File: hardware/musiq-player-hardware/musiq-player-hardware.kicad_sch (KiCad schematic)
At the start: 16 parts, among them SW1 SW_MEC_5E, SW2 SW_MEC_5E, SW3 SW_MEC_5E, SW4 SW_MEC_5E, SW5 SW_MEC_5E, U2 ESP32-PICO-D4

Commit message: adds sd card module and esp-pico-d4
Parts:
- removed U2: ESP32-PICO-D4, Package_DFN_QFN:QFN-48-1EP_7x7mm_P0.5mm_EP5.3x5.3mm, symbol RF_Module:ESP32-PICO-D4
- added C6, C7: 100nF, symbol Device:C_Small
- added J1: Micro_SD_Card, symbol Connector:Micro_SD_Card
- added R6, R7, R8, R9: 3.3k, symbol Device:R_US
- added U1: 74LVC125, symbol 74xx:74LVC125
- added U3: ~, symbol custom-modules:OLED-0.96{dblquote}
- added U4: ESP32-PICO-D4, Package_DFN_QFN:QFN-48-1EP_7x7mm_P0.5mm_EP5.3x5.3mm, symbol RF_Module:ESP32-PICO-D4
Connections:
- net +3V3: now also C6.1, C7.1, J1.4 (VDD), U1.14 (VCC), U4.1 (VDDA), U4.3 (VDDA3P3), U4.4 (VDDA3P3), U4.43 (VDDA), U4.46 (VDDA)
- net GND: now also C6.2, C7.2, J1.6 (VSS), J1.9 (SHIELD), U1.1, U1.10, U1.13, U1.4, U1.7 (GND), U4.49 (GND)
- new net: J1.2 (DAT3/CD), U1.8
- new net: R8.2, U1.9
- new net: R7.2, U1.5
- new net: R6.2, U1.2
- new net: J1.3 (CMD), U1.3
- new net: J1.7 (DAT0), R9.1
- new net: R9.2, U1.12
- new net: J1.5 (CLK), U1.6
- new net CS: R8.1
- new net MISO: U1.11
- new net MOSI: R6.1, R7.1
- no-connect marks 10 -> 12
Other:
- note removed: "OLED"
- note removed: "SDCARD MODULE"
- moved on the sheet: C1, C2, C3, C4, C5, R1, R2, R3, R4, R5, SW1, SW2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

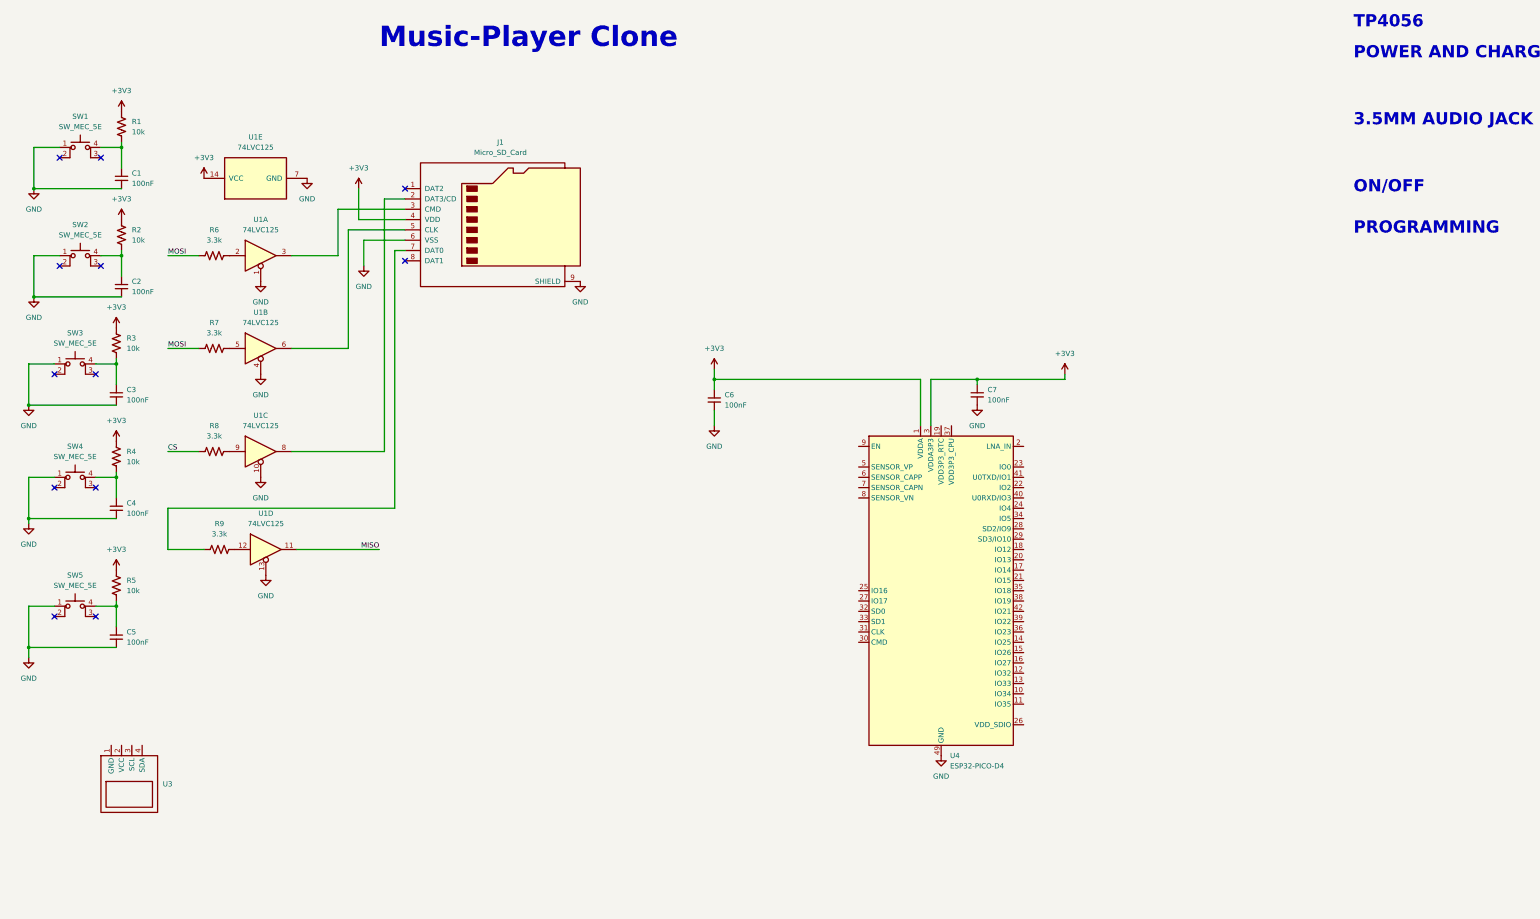
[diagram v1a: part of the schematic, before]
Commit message: adds on/off switch schematic
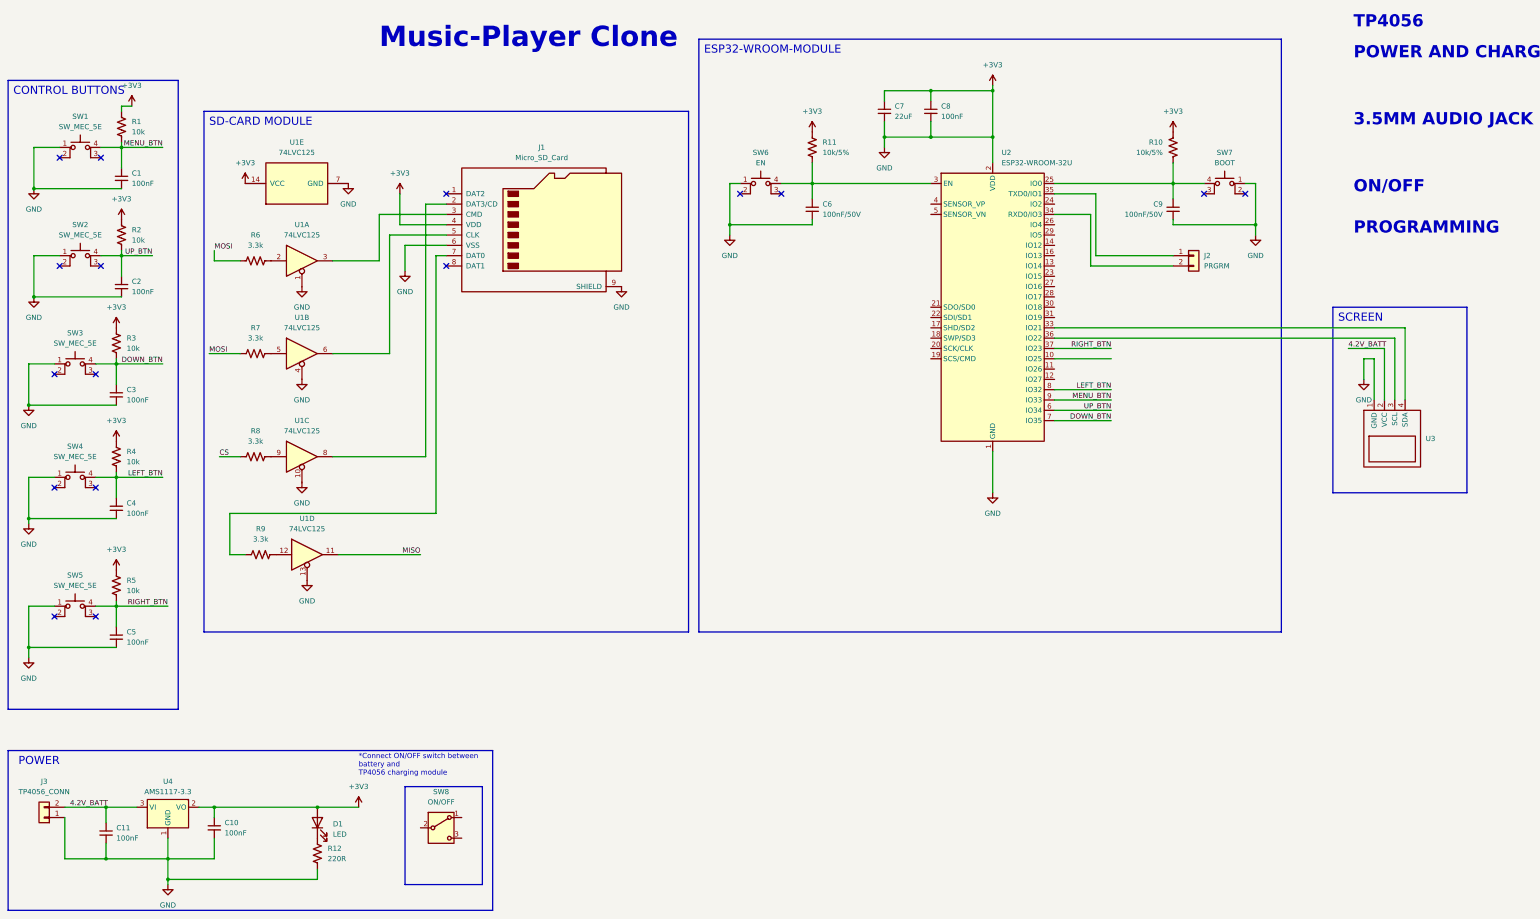
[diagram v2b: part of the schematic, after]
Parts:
- removed U4: ESP32-PICO-D4, Package_DFN_QFN:QFN-48-1EP_7x7mm_P0.5mm_EP5.3x5.3mm, symbol RF_Module:ESP32-PICO-D4
- added C10, C11, C8: 100nF, symbol Device:C_Small
- added C9: 100nF/50V, symbol Device:C_Small
- added D1: LED, symbol Device:LED
- added J2: PRGRM, symbol Connector_Generic:Conn_01x02
- added J3: TP4056_CONN, symbol Connector_Generic:Conn_01x02
- added R10, R11: 10k/5%, symbol Device:R_US
- added R12: 220R, symbol Device:R_US
- added SW6: EN, symbol Switch:SW_MEC_5E
- added SW7: BOOT, symbol Switch:SW_MEC_5E
- added SW8: ON/OFF, symbol Switch:SW_SPDT
- added U2: ESP32-WROOM-32U, RF_Module:ESP32-WROOM-32U, symbol RF_Module:ESP32-WROOM-32U
- added U4: AMS1117-3.3, Package_TO_SOT_SMD:SOT-223-3_TabPin2, symbol Regulator_Linear:AMS1117-3.3
- C6: value 100nF -> 100nF/50V
- C7: value 100nF -> 22uF
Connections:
- net GND is gone; now on net +3V3: C1.2, C2.2, C3.2, C4.2, C5.2, C6.2, C7.2, J1.6 (VSS), J1.9 (SHIELD), SW1.1, SW2.1, SW3.1, SW4.1, SW5.1, U1.1, U1.10, U1.13, U1.4, U1.7 (GND)
- net +3V3: now also U3.1 (GND), C10.1, C10.2, C11.2, C8.1, C8.2, C9.2, D1.2 (A), J3.1 (Pin_1), R10.1, R11.1, R12.2, SW6.1, SW7.1, U2.1 (GND), U2.15 (GND), U2.2 (VDD), U2.38 (GND), U2.39 (GND), U4.1 (GND), U4.2 (VO); no longer C6.1
- net RIGHT_BTN: now reaches C5.1, R5.2, SW5.4 (A)
- net RIGHT_BTN: now also U2.37 (IO23)
- net LEFT_BTN: now reaches C4.1, R4.2, SW4.4 (A)
- net LEFT_BTN: now also U2.8 (IO32)
- net UP_BTN: now reaches C2.1, R2.2, SW2.4 (A)
- net UP_BTN: now also U2.6 (IO34)
- net MENU_BTN: now reaches C1.1, R1.2, SW1.4 (A)
- net MENU_BTN: now also U2.9 (IO33)
- net DOWN_BTN: now reaches C3.1, R3.2, SW3.4 (A)
- net DOWN_BTN: now also U2.7 (IO35)
- net 4.2V_BATT: now reaches U3.2 (VCC)
- net 4.2V_BATT: now also C11.1, J3.2 (Pin_2), U4.3 (VI)
- net at U3.3 (SCL): now also U2.36 (IO22)
- net at U3.4 (SDA): now also U2.33 (IO21)
- new net: C6.1, R11.2, SW6.4 (A), U2.3 (EN)
- new net: D1.1 (K), R12.1
- new net: C9.1, R10.2, SW7.4 (A), U2.25 (IO0)
- new net: J2.1 (Pin_1), U2.35 (TXD0/IO1)
- new net: J2.2 (Pin_2), U2.34 (RXD0/IO3)
- no-connect marks 12 -> 16
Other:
- note added: "*Connect ON/OFF switch between battery and TP4056 charging module"
- note added: "CONTROL BUTTONS"
- note added: "ESP32-WROOM-MODULE"
- note added: "POWER"
- note added: "SCREEN"
- note added: "SD-CARD MODULE"
- moved on the sheet: J1, R6, R7, R8, R9, U1A, U1B, U1C, U1D, U1E, U3

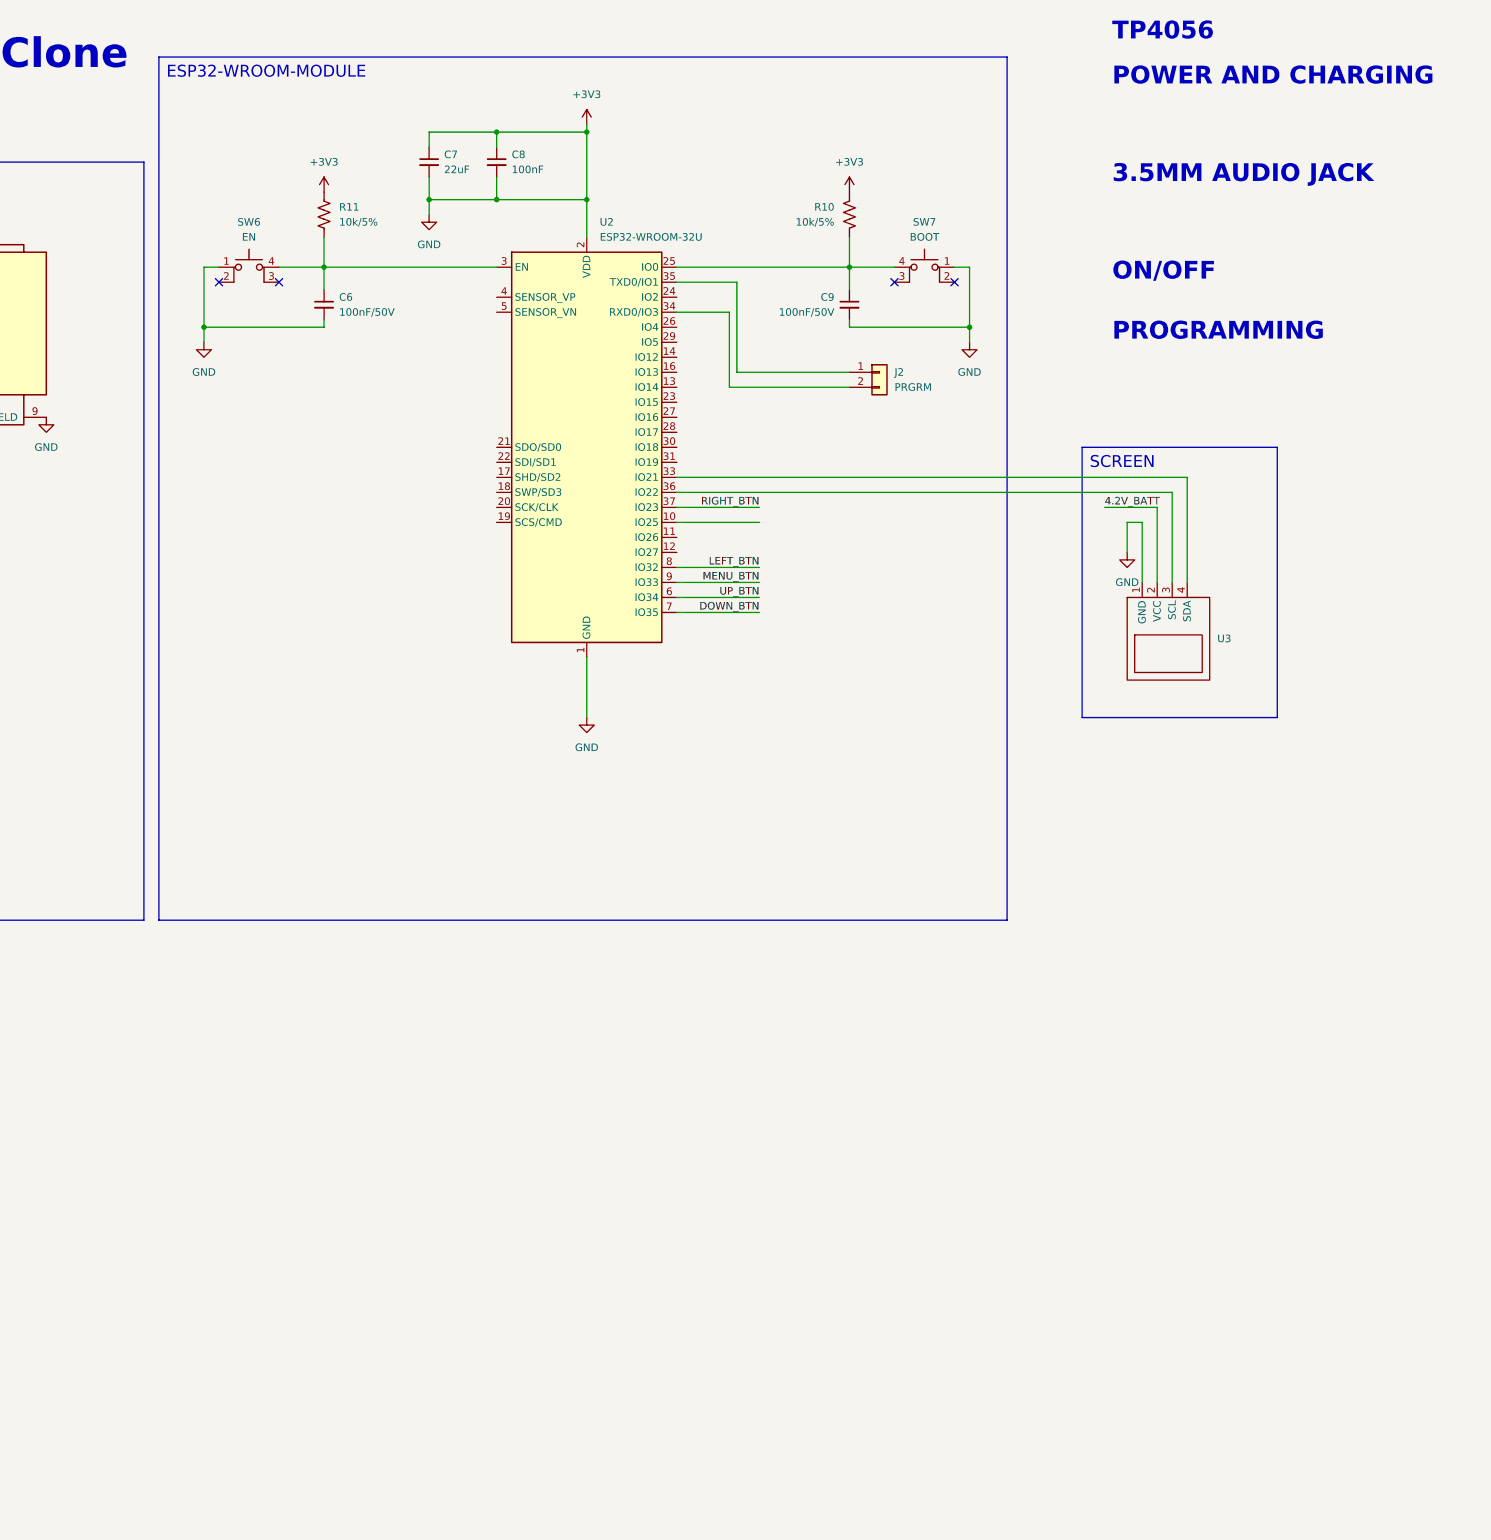
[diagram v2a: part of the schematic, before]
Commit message: adds esp32-c3 schematic
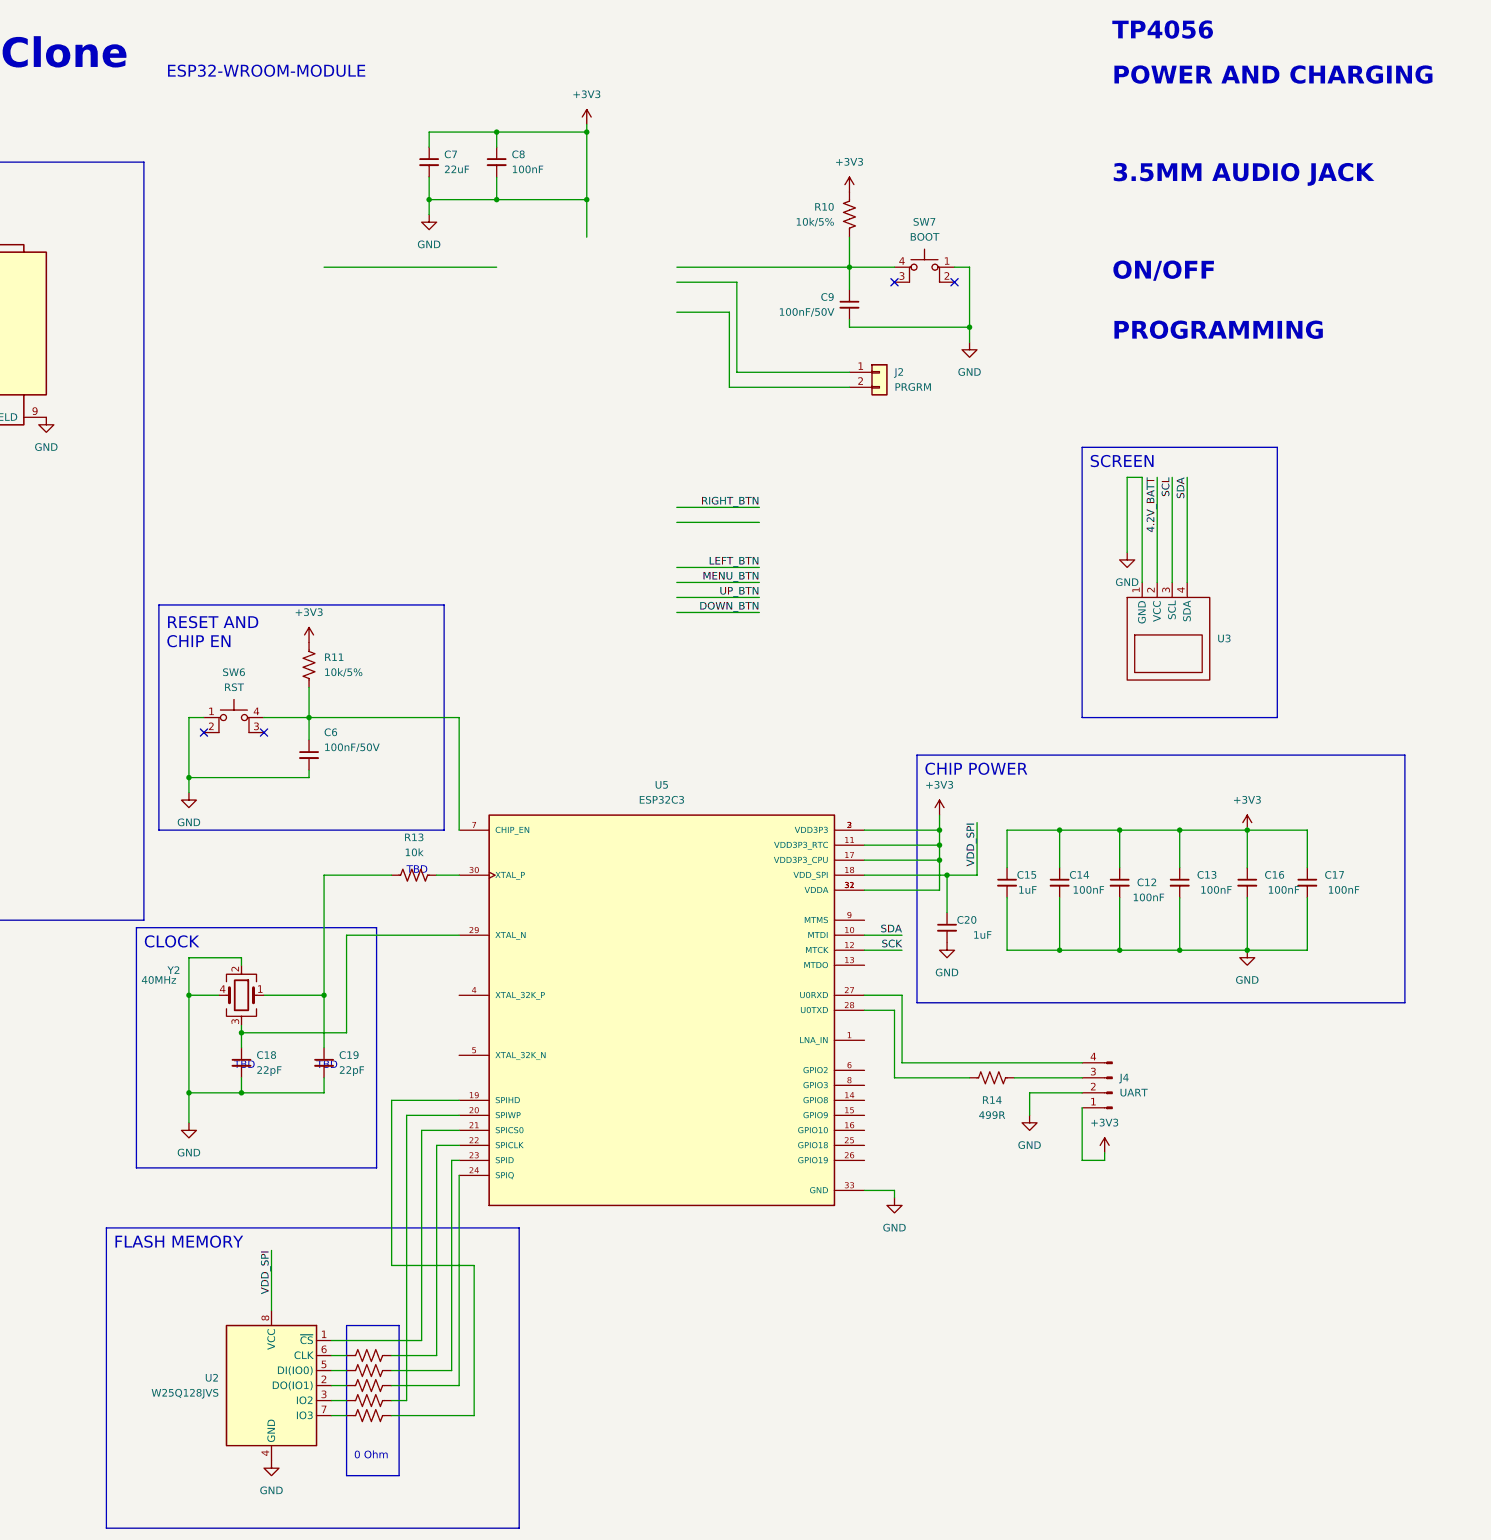
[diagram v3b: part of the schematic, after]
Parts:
- removed U2: ESP32-WROOM-32U, RF_Module:ESP32-WROOM-32U, symbol RF_Module:ESP32-WROOM-32U
- added C12, C13, C14, C16, C17: 100nF, symbol Device:C_Small
- added C15, C20: 1uF, symbol Device:C_Small
- added C18, C19: 22pF, symbol Device:C_Small
- added J4: UART, symbol Connector:Conn_01x04_Pin
- added R13, R16, R17, R18, R19, R20: 10k, symbol Device:R_US
- added R14: 499R, symbol Device:R_US
- added U2: W25Q128JVS, Package_SO:SOIC-8_5.23x5.23mm_P1.27mm, symbol Memory_Flash:W25Q128JVS
- added U5: ESP32C3, ESP32C3:QFN32_5X5MM, symbol ESP32C3:ESP32C3
- added Y2: 40MHz, symbol Device:Crystal_GND23
- SW6: value EN -> RST
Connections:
- net +3V3: now also C12.1, C12.2, C13.1, C13.2, C14.1, C14.2, C15.1, C15.2, C16.1, C16.2, C17.1, C17.2, C18.2, C19.2, C20.2, J4.1 (Pin_1), J4.2 (Pin_2), U2.4 (GND), U5.11 (VDD3P3_RTC), U5.17 (VDD3P3_CPU), U5.2 (VDD3P3), U5.3 (VDD3P3), U5.31 (VDDA), U5.32 (VDDA), U5.33 (GND), Y2.2, Y2.4
- net at C6.1, R11.2, SW6.4 (A): now also U5.7 (CHIP_EN)
- net SCL: now reaches U3.3 (SCL)
- net SDA: now reaches U3.4 (SDA)
- net SDA: now also U5.10 (MTDI)
- new net: C19.1, R13.1, Y2.1
- new net: R13.2, U5.30 (XTAL_P)
- new net: C18.1, U5.29 (XTAL_N), Y2.3
- new net: R17.1, U2.5 (DI(IO0))
- new net: R17.2, U5.23 (SPID)
- new net: R18.1, U2.2 (DO(IO1))
- new net: R18.2, U5.24 (SPIQ)
- new net: U2.1 (~{CS}), U5.21 (SPICS0)
- new net: R19.1, U2.3 (IO2)
- new net: R16.1, U2.6 (CLK)
- new net: R20.1, U2.7 (IO3)
- new net: R14.1, U5.28 (U0TXD)
- new net: J4.3 (Pin_3), R14.2
- new net: R19.2, U5.20 (SPIWP)
- new net: R16.2, U5.22 (SPICLK)
- new net: J4.4 (Pin_4), U5.27 (U0RXD)
- new net: R20.2, U5.19 (SPIHD)
- new net SCK: U5.12 (MTCK)
- new net VDD_SPI: C20.1, U2.8 (VCC), U5.18 (VDD_SPI)
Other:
- note added: "0 Ohm"
- note added: "CHIP POWER"
- note added: "CLOCK"
- note added: "FLASH MEMORY"
- note added: "RESET AND CHIP EN"
- note added: "TBD"

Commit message: complete schematic diagram
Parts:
- removed J2: PRGRM, symbol Connector_Generic:Conn_01x02
- removed R10: 10k/5%, symbol Device:R_US
- removed SW7: BOOT, symbol Switch:SW_MEC_5E
- added C21: 220pF, symbol Device:C_Small
- added FB1, FB2: FerriteBead, symbol Device:FerriteBead
- added J2: AudioJack3, symbol Connector_Audio:AudioJack3
- added U6: MAX98357AETE, MAX98357AETE:QFN50P300X300X80-17N, symbol MAX98357AETE:MAX98357AETE
- C7: value 22uF -> 10uF
- C8: value 100nF -> 0.1uF
- C9: value 100nF/50V -> 220pF
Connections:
- net CS is gone; now on net SD_CS: R8.1
- net MISO is gone; now on net SD_MISO: U1.11
- net SCK is gone; now on net SD_SCK: U5.12 (MTCK)
- net +3V3: now also U6.7 (VDD), U6.8 (VDD); no longer C1.2, C10.2, C11.2, C12.2, C13.2, C14.2, C15.2, C16.2, C17.2, C18.2, C19.2, C2.2, C20.2, C3.2, C4.2, C5.2, C6.2, C7.2, C8.2, C9.2, J1.6 (VSS), J1.9 (SHIELD), J3.1 (Pin_1), J4.2 (Pin_2), R12.2, SW1.1, SW2.1, SW3.1, SW4.1, SW5.1, SW6.1, U1.1, U1.10, U1.13, U1.4, U1.7 (GND), U2.4 (GND), U3.1 (GND), U4.1 (GND), U5.33 (GND), Y2.2, Y2.4
- net DOWN_BTN: now also U5.26 (GPIO19)
- net LEFT_BTN: now also U5.15 (GPIO9)
- net MENU_BTN: now also U5.8 (GPIO3)
- net RIGHT_BTN: now also U5.14 (GPIO8)
- net SCL: now also U5.9 (MTMS)
- net UP_BTN: now also U5.25 (GPIO18)
- net AUD_P: now reaches C9.1
- net AUD_P: now also FB2.2, J2.T
- net BCLK: now reaches U5.1 (LNA_IN)
- net BCLK: now also U6.16 (BCLK)
- net SD_MOSI: now reaches U5.13 (MTDO)
- net SD_MOSI: now also R6.1
- net SD_CS: now reaches U5.16 (GPIO10)
- net DIN: now reaches U5.4 (XTAL_32K_P)
- net DIN: now also U6.1 (DIN)
- net LRCLK: now reaches U5.5 (XTAL_32K_N)
- net LRCLK: now also U6.14 (LRCLK)
- net SD_MISO: now reaches U5.6 (GPIO2)
- net MOSI renamed SD_SCK
- net SD_SCK: no longer R6.1
- new net: FB2.1, U6.9 (OUTP)
- new net: C21.1, FB1.1, U6.10 (OUTN)
- new net AUD_N: FB1.2, J2.R
- new net GND: C1.2, C10.2, C11.2, C12.2, C13.2, C14.2, C15.2, C16.2, C17.2, C18.2, C19.2, C2.2, C20.2, C21.2, C3.2, C4.2, C5.2, C6.2, C7.2, C8.2, C9.2, J1.6 (VSS), J1.9 (SHIELD), J2.S, J3.1 (Pin_1), J4.2 (Pin_2), R12.2, SW1.1, SW2.1, SW3.1, SW4.1, SW5.1, SW6.1, U1.1, U1.10, U1.13, U1.4, U1.7 (GND), U2.4 (GND), U3.1 (GND), U4.1 (GND), U5.33 (GND), U6.11 (GND), U6.15 (GND), U6.2 (GAIN_SLOT), U6.3 (GND), Y2.2, Y2.4
- no-connect marks 16 -> 15
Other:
- note added: "AUDIO OUT"
- note added: "Connecting Gain to GND sets gain to 12dB"
- note added: "Ferrite - select w/high Z at high F, low-Z at low F. Try to block everything >1MHz or so"
- note added: "UART 0"
- note removed: "3.5MM AUDIO JACK"
- note removed: "ESP32-WROOM-MODULE"
- note removed: "ON/OFF"
- note removed: "POWER AND CHARGING"
- note removed: "PROGRAMMING"
- note removed: "TP4056"
